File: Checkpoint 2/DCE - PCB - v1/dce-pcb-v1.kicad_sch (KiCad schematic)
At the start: 56 parts, among them J2 Conn_01x02_Socket

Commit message: pcb actualizado con recomendaciones de julio
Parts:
- removed C7, C8: 10u, Capacitor_THT:CP_Radial_D5.0mm_P2.50mm, symbol Device:C
- added C10, C2, C9: 10n, Capacitor_THT:C_Disc_D3.4mm_W2.1mm_P2.50mm, symbol Device:C
- added J3: Conn_01x02_Socket, Connector_PinHeader_2.54mm:PinHeader_1x02_P2.54mm_Vertical, symbol Connector:Conn_01x02_Socket
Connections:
- net +VPOSA: now also C9.1
- net -VPOSA: now also C10.1
- net 0: now also C10.2, C2.2, C9.2
- net Vref: now also J?.6 (Pin_6); no longer J?.5 (Pin_5)
- net Vreg: now also C2.1, J3.1 (Pin_1)
- net Vsel: now also J?.5 (Pin_5), J3.2 (Pin_2); no longer J?.6 (Pin_6)
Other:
- moved on the sheet: C4, C5, C6, J?

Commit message: pcb_para_imprimir
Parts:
- added R24, R25: 10, Resistor_THT:R_Axial_DIN0207_L6.3mm_D2.5mm_P7.62mm_Horizontal, symbol Device:R
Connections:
- new net: Q?.3 (E), R25.2
- new net: Q?.1 (C), R24.2, R25.1
- new net: Q?.3 (E), R24.1
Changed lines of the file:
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@@
 	)
 	(junction
-		(at 78.74 77.47)
-		(diameter 0)
-		(color 0 0 0 0)
-	)
-	(junction
 		(at 279.4 161.29)
 		(diameter 0)
@@
 	)
 	(junction
+		(at 78.74 81.28)
+		(diameter 0)
+		(color 0 0 0 0)
+	)
+	(junction
 		(at 82.55 119.38)
 		(diameter 0)
@@
 	(wire
 		(pts
-			(xy 78.74 88.9) (xy 78.74 77.47)
-		)
-		(stroke
-			(width 0.1524)
-			(type solid)
-		)
-	)
-	(wire
-		(pts
 			(xy 181.61 83.82) (xy 160.02 83.82)
 		)
@@
 	(wire
 		(pts
-			(xy 78.74 77.47) (xy 69.85 77.47)
-		)
-		(stroke
-			(width 0.1524)
-			(type solid)
-		)
-	)
-	(wire
-		(pts
 			(xy 87.63 31.75) (xy 87.63 26.67)
 		)
@@
 	(wire
 		(pts
-			(xy 87.63 77.47) (xy 78.74 77.47)
-		)
-		(stroke
-			(width 0.1524)
-			(type solid)
-		)
-	)
-	(wire
-		(pts
 			(xy 81.28 146.05) (xy 81.28 147.32)
 		)
@@
 	(wire
 		(pts
+			(xy 77.47 81.28) (xy 78.74 81.28)
+		)
+		(stroke
+			(width 0)
+			(type default)
+		)
+	)
+	(wire
+		(pts
 			(xy 266.7 172.72) (xy 267.97 172.72)
 		)
@@
 	(wire
 		(pts
+			(xy 78.74 81.28) (xy 80.01 81.28)
+		)
+		(stroke
+			(width 0)
+			(type default)
+		)
+	)
+	(wire
+		(pts
 			(xy 238.76 87.63) (xy 240.03 87.63)
 		)
@@
 	(wire
 		(pts
+			(xy 87.63 77.47) (xy 87.63 81.28)
+		)
+		(stroke
+			(width 0)
+			(type default)
+		)
+	)
+	(wire
+		(pts
 			(xy 41.91 85.09) (xy 30.48 85.09)
 		)
@@
 	(wire
 		(pts
+			(xy 78.74 81.28) (xy 78.74 88.9)
+		)
+		(stroke
+			(width 0)
+			(type default)
+		)
+	)
+	(wire
+		(pts
 			(xy 69.85 67.31) (xy 69.85 58.42)
 		)
@@
 	(wire
 		(pts
-			(xy 69.85 77.47) (xy 69.85 74.93)
+			(xy 69.85 74.93) (xy 69.85 81.28)
 		)
 		(stroke
@@
 	)
 	(symbol
+		(lib_id "Device:R")
+		(at 73.66 81.28 90)
+		(unit 1)
+		(exclude_from_sim no)
+		(in_bom yes)
+		(on_board yes)
+		(dnp no)
+		(fields_autoplaced yes)
+		(property "Reference" "R24"
+			(at 73.66 74.93 90)
+			(effects
+				(font
+					(size 1.27 1.27)
+				)
+			)
+		)
+		(property "Value" "10"
+			(at 73.66 77.47 90)
+			(effects
+				(font
+					(size 1.27 1.27)
+				)
+			)
+		)
+		(property "Footprint" "Resistor_THT:R_Axial_DIN0207_L6.3mm_D2.5mm_P7.62mm_Horizontal"
+			(at 73.66 83.058 90)
+			(effects
+				(font
+					(size 1.27 1.27)
+				)
+				(hide yes)
+			)
+		)
+		(property "Datasheet" "~"
+			(at 73.66 81.28 0)
+			(effects
+				(font
+					(size 1.27 1.27)
+				)
+				(hide yes)
+			)
+		)
+		(property "Description" "Resistor"
+			(at 73.66 81.28 0)
+			(effects
+				(font
+					(size 1.27 1.27)
+				)
+				(hide yes)
+			)
+		)
+		(pin "2"
+		)
+		(pin "1"
+		)
+		(instances
+			(project ""
+				(path "/e6ededfa-1272-42e1-ab55-13acb1f29d6e"
+					(reference "R24")
+					(unit 1)
+				)
+			)
+		)
+	)
+	(symbol
 		(lib_id "ltspice:GND")
 		(at 116.84 151.13 0)
@@
 					(unit 1)
 				)
+			)
+		)
+	)
+	(symbol
+		(lib_id "Device:R")
+		(at 83.82 81.28 90)
+		(unit 1)
+		(exclude_from_sim no)
+		(in_bom yes)
+		(on_board yes)
+		(dnp no)
+		(fields_autoplaced yes)
+		(property "Reference" "R25"
+			(at 83.82 74.93 90)
+			(effects
+				(font
+					(size 1.27 1.27)
+				)
+			)
+		)
+		(property "Value" "10"
+			(at 83.82 77.47 90)
+			(effects
+				(font
+					(size 1.27 1.27)
+				)
+			)
+		)
+		(property "Footprint" "Resistor_THT:R_Axial_DIN0207_L6.3mm_D2.5mm_P7.62mm_Horizontal"
+			(at 83.82 83.058 90)
+			(effects
+				(font
+					(size 1.27 1.27)
+				)
+				(hide yes)
+			)
+		)
+		(property "Datasheet" "~"
+			(at 83.82 81.28 0)
+			(effects
+				(font
+					(size 1.27 1.27)
+				)
+				(hide yes)
+			)
+		)
+		(property "Description" "Resistor"
+			(at 83.82 81.28 0)
+			(effects
+				(font
+					(size 1.27 1.27)
+				)
+				(hide yes)
+			)
+		)
+		(pin "2"
+		)
+		(pin "1"
+		)
+		(instances
+			(project "dce-pcb-v1"
+				(path "/e6ededfa-1272-42e1-ab55-13acb1f29d6e"
+					(reference "R25")
+					(unit 1)
+				)

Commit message: ojala no rompa todo
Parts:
- added C7: C, Capacitor_THT:CP_Radial_D5.0mm_P2.50mm, symbol Device:C
- added R26, R27: 1k, Resistor_THT:R_Axial_DIN0207_L6.3mm_D2.5mm_P7.62mm_Horizontal, symbol Device:R
- R?: footprint Resistor_THT:R_Axial_DIN0207_L6.3mm_D2.5mm_P7.62mm_Horizontal -> Resistor_THT:R_Axial_Power_L25.0mm_W6.4mm_P30.48mm
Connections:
- net 0: now also C7.2, R26.2
- net Vsel: now also R27.2; no longer M?.2 (G)
- new net: C7.1, M?.2 (G), R26.1, R27.1

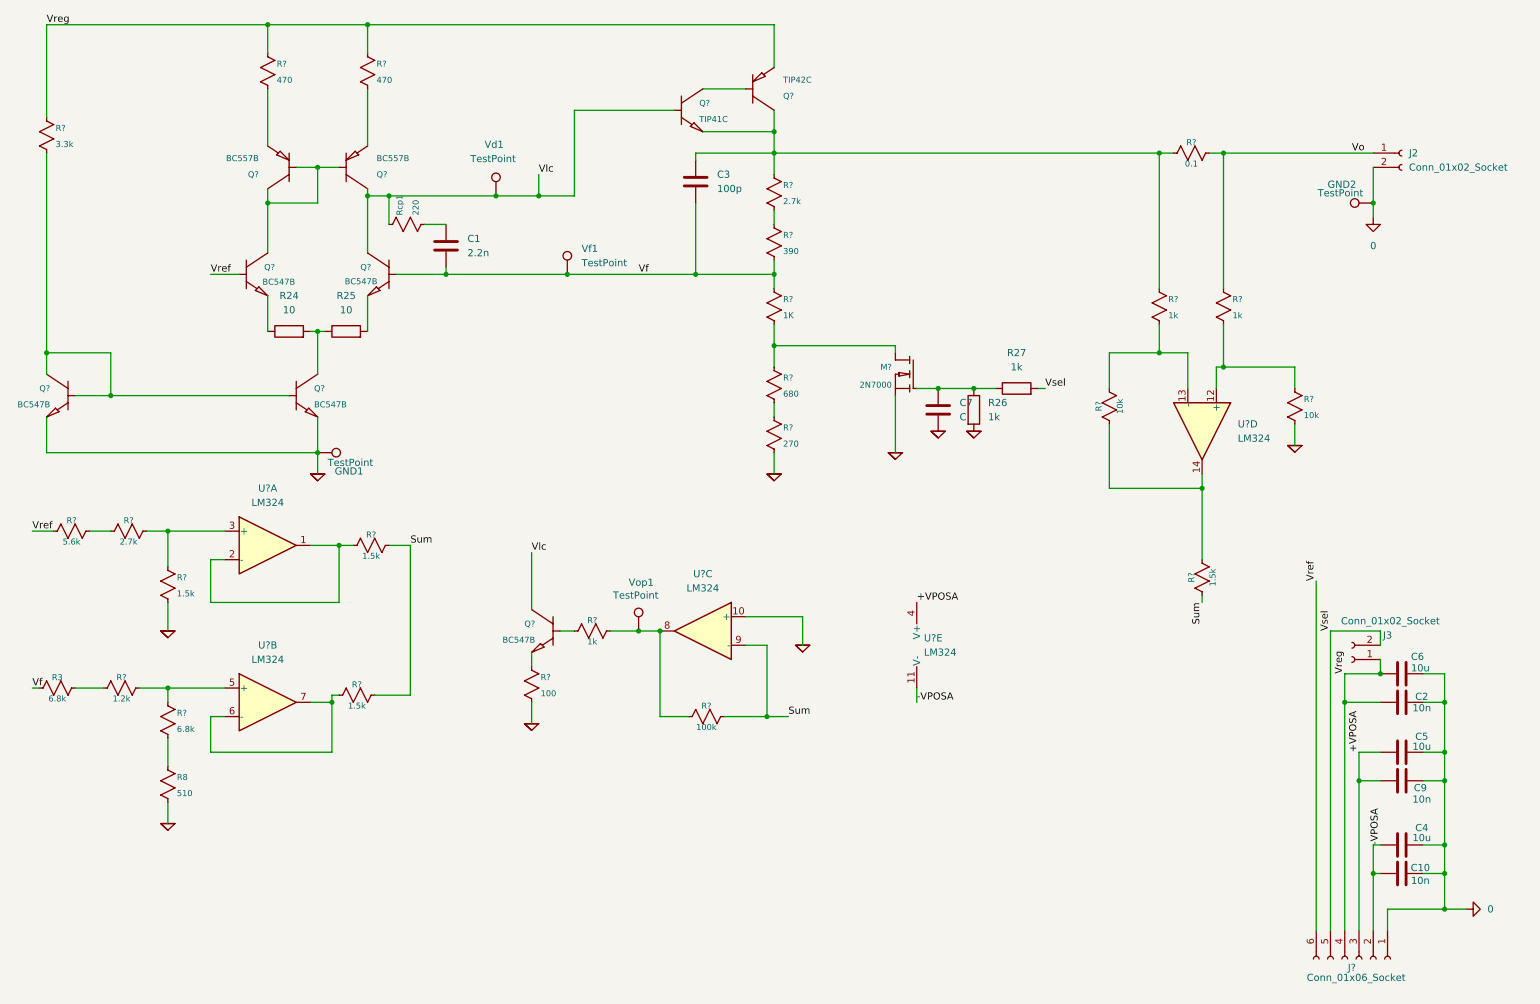
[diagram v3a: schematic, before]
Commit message: actualiza spice con los cambios en el pcb
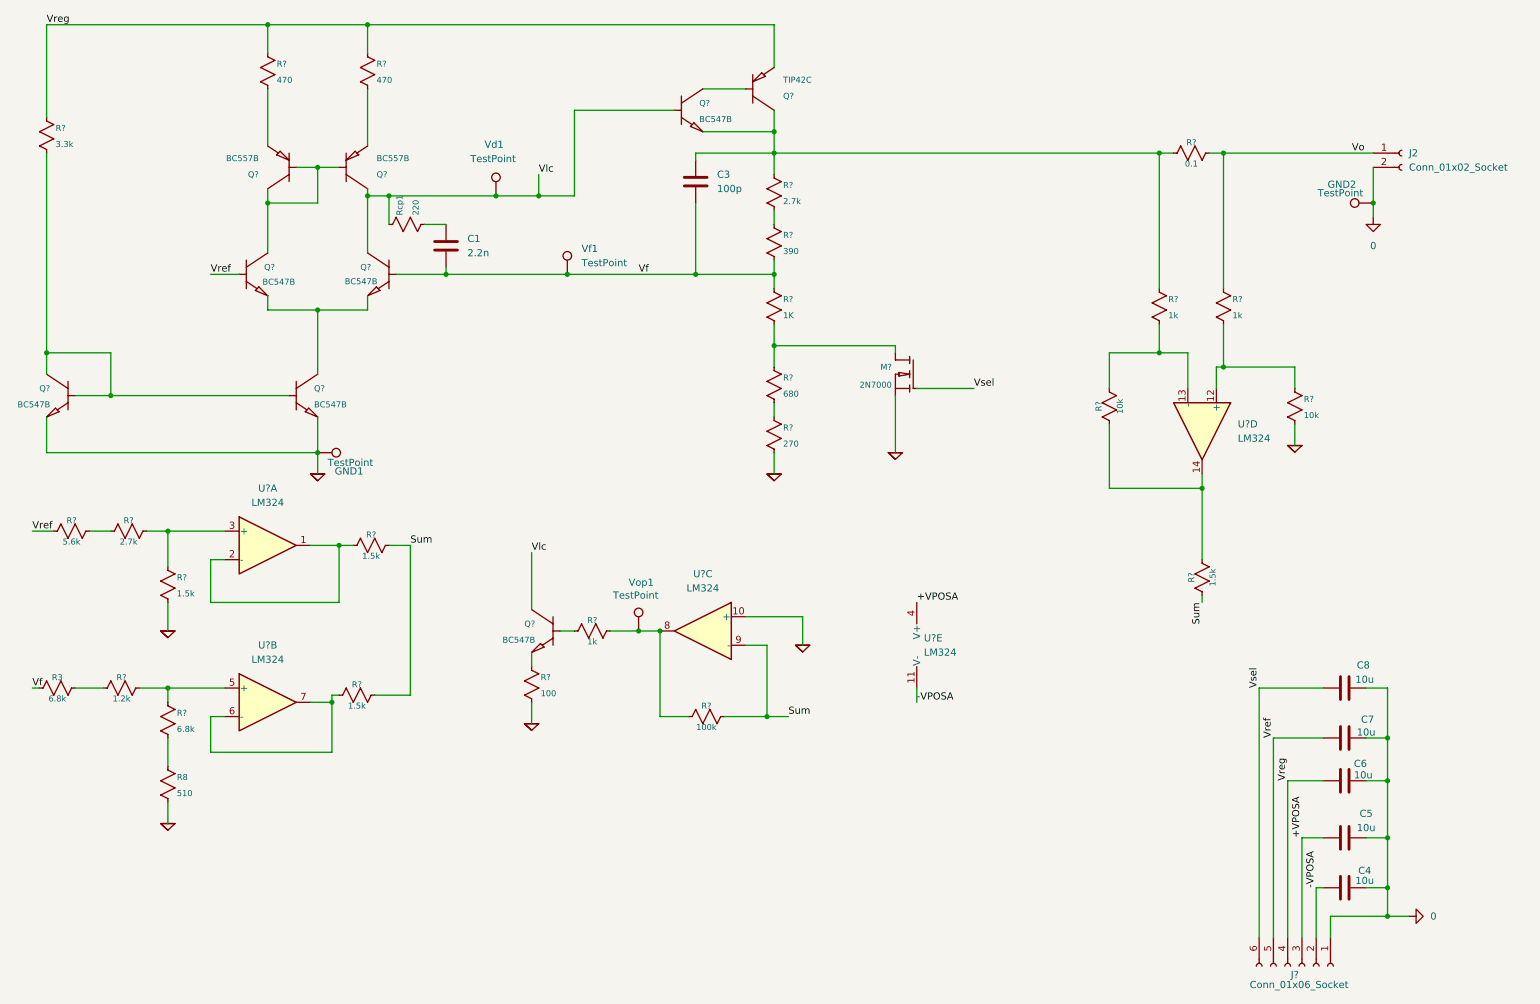
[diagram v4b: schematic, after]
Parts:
- removed C10, C2, C9: 10n, Capacitor_THT:C_Disc_D3.4mm_W2.1mm_P2.50mm, symbol Device:C
- removed J3: Conn_01x02_Socket, Connector_PinHeader_2.54mm:PinHeader_1x02_P2.54mm_Vertical, symbol Connector:Conn_01x02_Socket
- removed R24, R25: 10, Resistor_THT:R_Axial_DIN0207_L6.3mm_D2.5mm_P7.62mm_Horizontal, symbol Device:R
- removed R26, R27: 1k, Resistor_THT:R_Axial_DIN0207_L6.3mm_D2.5mm_P7.62mm_Horizontal, symbol Device:R
- added C8: 10u, Capacitor_THT:CP_Radial_D5.0mm_P2.50mm, symbol Device:C
- C7: value C -> 10u
- Q?: value TIP41C -> BC547B
- R?: footprint Resistor_THT:R_Axial_Power_L25.0mm_W6.4mm_P30.48mm -> Resistor_THT:R_Axial_DIN0207_L6.3mm_D2.5mm_P7.62mm_Horizontal
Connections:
- net 0: now also C8.2
- net Vref: now also C7.1, J?.5 (Pin_5); no longer J?.6 (Pin_6)
- net Vsel: now also J?.6 (Pin_6), M?.2 (G), C8.1; no longer J?.5 (Pin_5)
- net at Q?.3 (E): now also Q?.1 (C), Q?.3 (E)
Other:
- moved on the sheet: C4, C5, C6, J?
